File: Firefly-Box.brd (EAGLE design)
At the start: 90 x 56 mm, 40 parts, among them U1 ATMEGA32U4-XUMU, U2 ATMEGA32U4-XUAU, Y1 16MHz KX-7

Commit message: Add power to wings
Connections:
- removed net 5V: CONN2.VUSB, U1.7
- new net 5V0: AH1.5V@2, AH2.5V@2, AL1.5V@2, AL2.5V@2, BUS1.5V@2, BUS2.5V@2, BUS3.5V@2, BUS4.5V@2, CONN2.VUSB, U1.7
- net 3V3: now also AH1.3V3@2, AH2.3V3@2, AL1.3V3@2, AL2.3V3@2, BUS1.3V3@2, BUS2.3V3@2, BUS3.3V3@2, BUS4.3V3@2
- net GND: now also AH1.GND@2, AH2.GND@2, AL1.GND@2, AL2.GND@2, BUS1.GND@2, BUS2.GND@2, BUS3.GND@2, BUS4.GND@2
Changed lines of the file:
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@@
 </polygon>
 <contactref element="CONN2" pad="GND"/>
-<wire x1="33.909" y1="37.973" x2="34.544" y2="39.243" width="0" layer="19" extent="1-1"/>
-<wire x1="30.734" y1="41.021" x2="34.544" y2="39.243" width="0" layer="19" extent="1-1"/>
-<wire x1="19.177" y1="24.765" x2="21.184" y2="24.867" width="0" layer="19" extent="1-1"/>
-<wire x1="25.364" y1="40.887" x2="28.194" y2="39.116" width="0" layer="19" extent="1-1"/>
-<wire x1="27.214" y1="43.187" x2="25.364" y2="40.887" width="0" layer="19" extent="1-1"/>
-<wire x1="26.543" y1="45.212" x2="27.214" y2="43.187" width="0" layer="19" extent="1-1"/>
-<wire x1="15.24" y1="22.987" x2="19.177" y2="24.765" width="0" layer="19" extent="1-1"/>
-<wire x1="13.986" y1="25.908" x2="15.24" y2="22.987" width="0" layer="19" extent="1-1"/>
-<wire x1="33.274" y1="28.4376" x2="26.289" y2="28.067" width="0" layer="19" extent="16-16"/>
-<wire x1="8.95" y1="26.34" x2="15.24" y2="22.987" width="0" layer="19" extent="1-1"/>
-<wire x1="13.555" y1="36.322" x2="18.584" y2="33.972" width="0" layer="19" extent="1-1"/>
-<wire x1="13.555" y1="40.132" x2="13.555" y2="36.322" width="0" layer="19" extent="1-1"/>
+<contactref element="AH1" pad="GND@2"/>
+<contactref element="AL1" pad="GND@2"/>
+<contactref element="AL2" pad="GND@2"/>
+<contactref element="AH2" pad="GND@2"/>
+<contactref element="BUS2" pad="GND@2"/>
+<contactref element="BUS1" pad="GND@2"/>
+<contactref element="BUS3" pad="GND@2"/>
+<contactref element="BUS4" pad="GND@2"/>
 </signal>
 <signal name="AREF" class="4">
@@
 <contactref element="R5" pad="1"/>
 <contactref element="CONN2" pad="D+"/>
-<wire x1="8.95" y1="27.94" x2="7.89" y2="20.828" width="0" layer="19" extent="1-1"/>
+<wire x1="7.89" y1="20.828" x2="8.95" y2="27.94" width="0" layer="19" extent="1-1"/>
 </signal>
 <signal name="N$2">
@@
 <wire x1="30.184" y1="26.772" x2="29.362" y2="26.772" width="0.254" layer="1"/>
 <wire x1="25.884" y1="34.012" x2="25.884" y2="33.247" width="0.254" layer="1"/>
+<contactref element="BUS1" pad="3V3@2"/>
+<contactref element="BUS2" pad="3V3@2"/>
+<contactref element="BUS3" pad="3V3@2"/>
+<contactref element="BUS4" pad="3V3@2"/>
+<contactref element="AL2" pad="3V3@2"/>
+<contactref element="AH2" pad="3V3@2"/>
+<contactref element="AL1" pad="3V3@2"/>
+<contactref element="AH1" pad="3V3@2"/>
+<wire x1="53.848" y1="44.45" x2="74.168" y2="44.45" width="0" layer="19" extent="1-1"/>
+<wire x1="48.768" y1="34.29" x2="53.848" y2="44.45" width="0" layer="19" extent="1-1"/>
+<wire x1="41.148" y1="41.91" x2="48.768" y2="34.29" width="0" layer="19" extent="1-1"/>
+<wire x1="38.608" y1="41.656" x2="41.148" y2="41.91" width="0" layer="19" extent="1-1"/>
 <wire x1="27.659" y1="27.972" x2="25.884" y2="33.247" width="0" layer="19" extent="1-1"/>
 <wire x1="21.884" y1="26.697" x2="27.659" y2="27.972" width="0" layer="19" extent="1-1"/>
 <wire x1="21.884" y1="26.3544" x2="21.884" y2="26.697" width="0" layer="19" extent="1-1"/>
-<wire x1="12.192" y1="39.004" x2="26.784" y2="36.817" width="0" layer="19" extent="1-1"/>
+<wire x1="15.748" y1="11.43" x2="17.145" y2="22.86" width="0" layer="19" extent="1-1"/>
+<wire x1="41.148" y1="21.59" x2="30.184" y2="26.772" width="0" layer="19" extent="1-1"/>
+<wire x1="48.768" y1="13.97" x2="41.148" y2="21.59" width="0" layer="19" extent="1-1"/>
+<wire x1="36.068" y1="11.43" x2="41.148" y2="21.59" width="0" layer="19" extent="1-1"/>
+<wire x1="12.192" y1="39.004" x2="25.884" y2="34.012" width="0" layer="19" extent="1-1"/>
 <wire x1="10.668" y1="39.004" x2="12.192" y2="39.004" width="0" layer="19" extent="1-1"/>
 <wire x1="11.43" y1="41.672" x2="12.192" y2="39.004" width="0" layer="19" extent="1-1"/>
@@
 <wire x1="21.109" y1="28.972" x2="43.688" y2="19.05" width="0" layer="19" extent="1-1"/>
 </signal>
-<signal name="5V" class="3">
+<signal name="5V0">
+<contactref element="AH2" pad="5V@2"/>
+<contactref element="AL2" pad="5V@2"/>
+<contactref element="AL1" pad="5V@2"/>
+<contactref element="AH1" pad="5V@2"/>
+<contactref element="BUS3" pad="5V@2"/>
+<contactref element="BUS4" pad="5V@2"/>
+<contactref element="BUS2" pad="5V@2"/>
+<contactref element="BUS1" pad="5V@2"/>
 <contactref element="CONN2" pad="VUSB"/>
 <contactref element="U1" pad="7"/>
+<wire x1="56.388" y1="44.45" x2="76.708" y2="44.45" width="0" layer="19" extent="1-1"/>
+<wire x1="48.768" y1="36.83" x2="56.388" y2="44.45" width="0" layer="19" extent="1-1"/>
+<wire x1="41.148" y1="39.37" x2="48.768" y2="36.83" width="0" layer="19" extent="1-1"/>
+<wire x1="27.659" y1="30.472" x2="41.148" y2="39.37" width="0" layer="19" extent="1-1"/>
+<wire x1="41.148" y1="19.05" x2="27.659" y2="30.472" width="0" layer="19" extent="1-1"/>
+<wire x1="48.768" y1="16.51" x2="41.148" y2="19.05" width="0" layer="19" extent="1-1"/>
+<wire x1="33.528" y1="11.43" x2="41.148" y2="19.05" width="0" layer="19" extent="1-1"/>
 <wire x1="8.95" y1="29.54" x2="27.659" y2="30.472" width="0" layer="19" extent="1-1"/>
+<wire x1="13.208" y1="11.43" x2="8.95" y2="29.54" width="0" layer="19" extent="1-1"/>
 </signal>
 </signals>

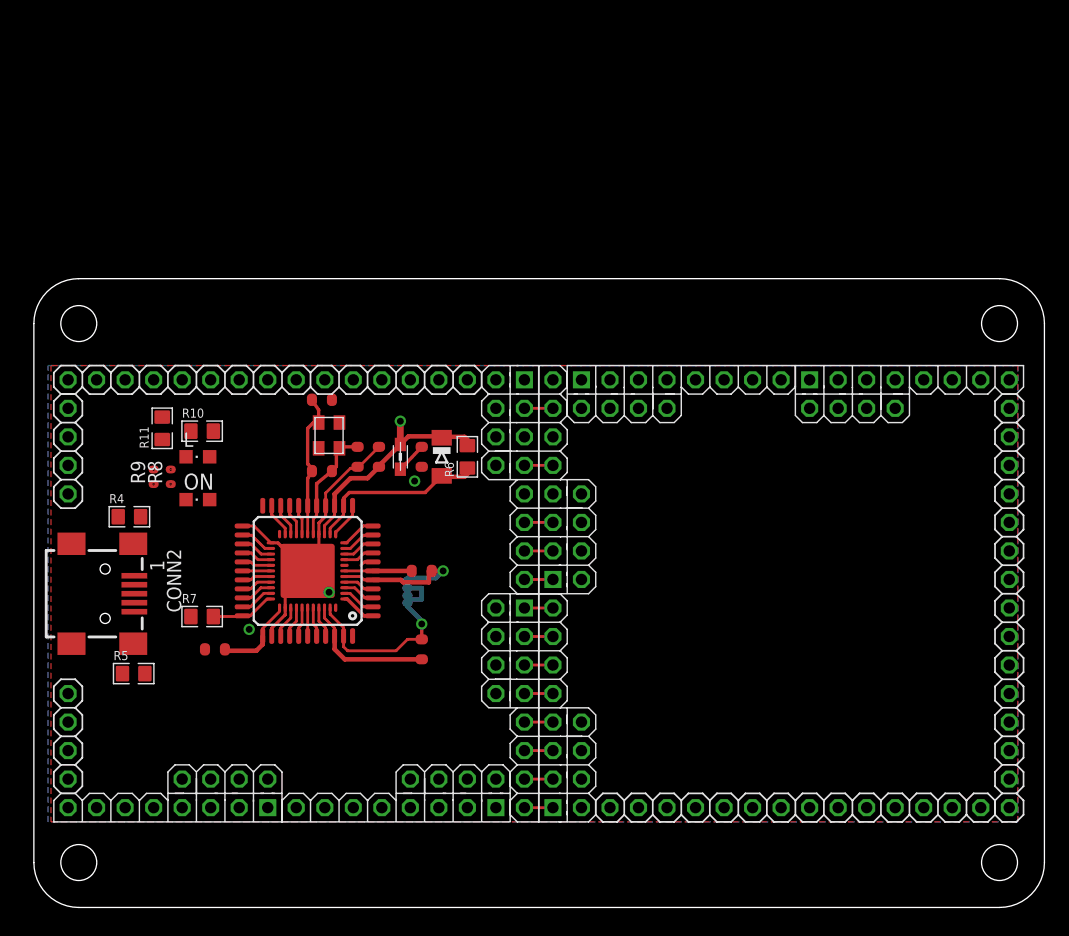
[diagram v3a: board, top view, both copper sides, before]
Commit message: Added Power and LiPo section.
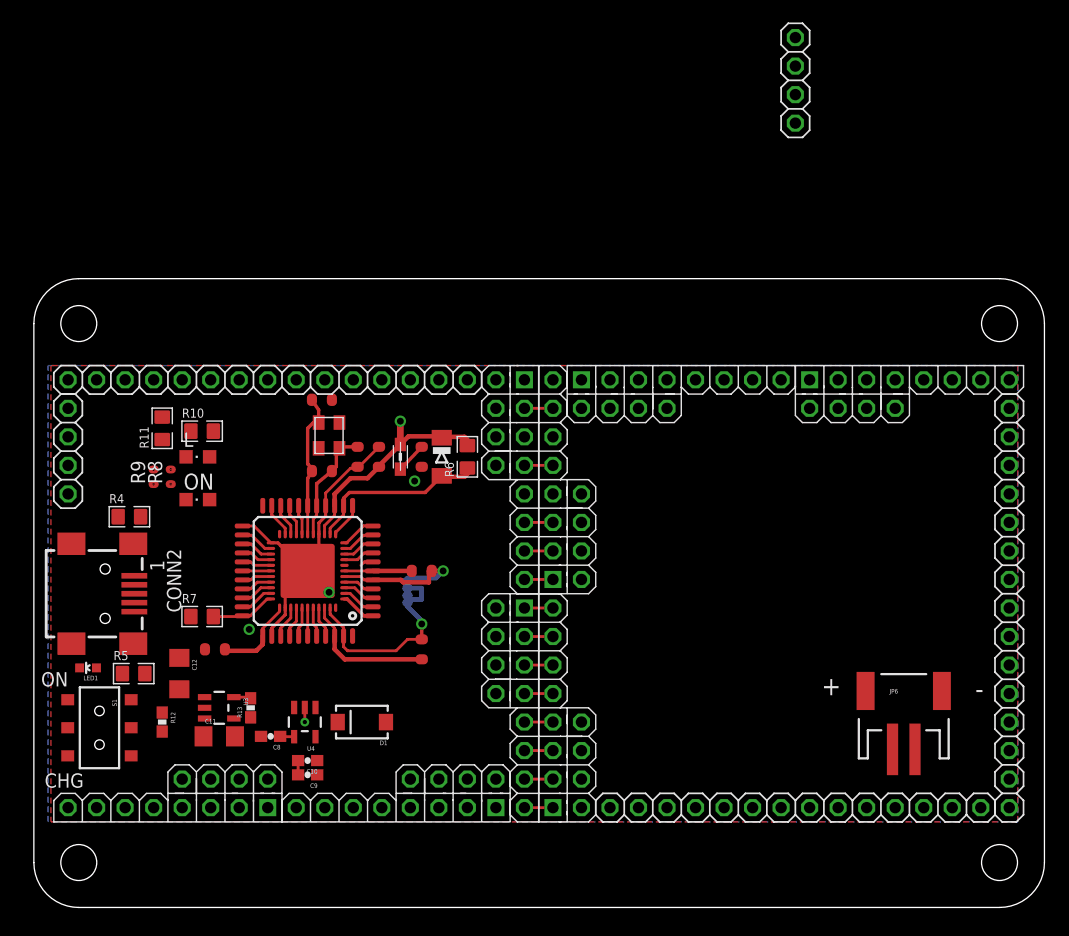
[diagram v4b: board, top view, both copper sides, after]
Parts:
- added C10: 4.7uF, SparkFun-Passives:0603-CAP
- added C11, C12: 4.7uF, SparkFun-Passives:1206
- added C8: 470pF, SparkFun-Passives:0603-CAP
- added C9: .1uF, SparkFun-Passives:0603-CAP
- added D1: B340A, SparkFun-DiscreteSemi:SMA-DIODE
- added JP6: JST-2, SparkFun-Connectors:JST-2-SMD
- added LED1: RED, SparkFun-LED:LED-0603
- added R12: 330, SparkFun-Passives:0603-RES
- added R13: 10k, SparkFun-Passives:0603-RES
- added S1: SWITCH-DPDTSMD, SparkFun-Electromechanical:AYZ0202
- added U3: MCP73831, SparkFun-PowerIC:SOT23-5
- added U4: MIC5219, SparkFun-PowerIC:SOT23-5
- moved JP5 87.2 mm to (67.8, 73.7)
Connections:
- new net N$1: S1.2, U4.3
- new net N$4: LED1.A, R12.1
- new net N$5: LED1.C, U3.1
- new net N$6: R13.2, U3.5
- new net N$8: C8.1, U4.4
- new net V_BATT: C12.2, D1.A, JP6.2, U3.3
- net 3V3: now also C10.2, C9.2, U4.5
- net 5V0: now also C11.2, D1.C, R12.2, S1.1, U3.4, U4.1
- net GND: now also C10.1, C11.1, C12.1, C8.2, C9.1, JP6.1, R13.1, S1.3, U3.2, U4.2
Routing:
- net N$8: track 0.00 -> 2.71 mm
- net 3V3: track 31.0 -> 32.5 mm
- net N$6: track 0.00 -> 1.51 mm
- net GND: track 35.9 -> 37.2 mm, vias 3 -> 4
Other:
- board text added: "+"
- board text added: "-"
- board text added: "CHG"
- board text added: "ON"

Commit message: Lots of routing done.
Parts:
- removed L: Yellow, led:CHIPLED_0805
- removed ON: Green, led:CHIPLED_0805
- removed R10, R11: 1K, GadgetFactory_6.0:0805
- moved R8 30.2 mm to (25.9, 11.4)
- moved R9 29.8 mm to (23.4, 11.4)
- moved R12 28.6 mm to (6.60, 44.7), turned to 0 degrees
- moved C9 27.8 mm to (19.4, 39.1), turned to 90 degrees
- moved C10 26.8 mm to (18.2, 39.1), turned to 90 degrees
- moved C11 26.0 mm to (14.2, 41.1)
- moved R13 26.0 mm to (17.0, 43.7)
- moved U3 26.0 mm to (14.2, 43.7)
- moved JP4 25.4 mm to (3.05, 15.2)
- moved D1 24.3 mm to (53.3, 14.0), turned to 270 degrees
- moved U4 23.8 mm to (14.2, 38.1), turned to 270 degrees
- moved LED1 23.4 mm to (3.56, 44.7)
- moved S1 22.9 mm to (5.33, 38.9)
- moved C12 22.0 mm to (10.4, 42.7)
- moved C8 21.7 mm to (14.2, 35.8)
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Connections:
- removed net N$2: L.A, R10.2
- removed net N$3: ON.A, R11.2
- removed net VUSB: U2.7
- net 3V3: no longer R11.1
- net 5V0: now also U2.7
- net D11*: now also AH1.5, AH2.2; no longer AH1.3, AH2.4
- net D12*: now also AL1.3, AL2.4; no longer AH1.4, AH2.3
- net D13*: now also AL1.4, AL2.3; no longer AH1.5, AH2.2
- net D3*: now also AH1.4, AH2.3; no longer AL1.3, AL2.4
- net D4*: now also AH1.3, AH2.4; no longer AL1.4, AL2.3, R10.1
- net GND: no longer L.C, ON.C
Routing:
- net SPI-CS4: track 0.00 -> 76.6 mm
- net 5V0: track 0.00 -> 73.8 mm, vias 0 -> 1
- net I2C-SCL: track 2.65 -> 64.8 mm, vias 0 -> 1
- net I2C-SDA: track 2.77 -> 59.7 mm, vias 0 -> 1
- net D15: track 5.07 -> 57.0 mm
- net RD+: track 2.77 -> 52.9 mm, vias 0 -> 2
- net AVCC: track 5.77 -> 53.5 mm, vias 0 -> 3
- net D12*: track 5.19 -> 51.2 mm, vias 0 -> 1
- net D11*: track 5.31 -> 49.2 mm
- net D3*: track 5.44 -> 47.5 mm
- net D13*: track 5.19 -> 46.3 mm, vias 0 -> 1
- net D4*: track 3.02 -> 42.4 mm
- net D0/RX: track 2.90 -> 42.0 mm, vias 0 -> 2
- net SPI-CS2: track 2.77 -> 41.5 mm, vias 0 -> 1
- net SPI-CS3: track 2.77 -> 40.9 mm, vias 0 -> 1
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- added copper zone on layer 1, net 3V3
- removed copper zone on layer 1, net GND

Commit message: Fully Routed
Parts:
- removed JP5: (no value), pinhead:1X04
- moved C10 0.72 mm to (17.7, 38.6)
- moved C9 0.51 mm to (19.4, 38.6)
- moved C11 0.25 mm to (14.2, 40.9)
- moved C12 0.25 mm to (10.4, 42.9)
- moved LED1 0.25 mm to (3.56, 44.5)
- moved R12 0.25 mm to (6.60, 44.5)
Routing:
- net SPI-MISO: track 3.15 -> 160.3 mm, vias 0 -> 5
- net I2C-SCL: track 64.8 -> 221.8 mm, vias 1 -> 7
- net V_BATT: track 3.12 -> 156.5 mm, vias 0 -> 4
- net 5V0: track 73.8 -> 223.0 mm, vias 1 -> 12
- net I2C-SDA: track 59.7 -> 196.3 mm, vias 1 -> 8
- net SPI-SCK: track 37.4 -> 173.6 mm, vias 0 -> 6
- net SPI-MOSI: track 32.4 -> 164.2 mm, vias 0 -> 2
- net 3V3: track 30.4 -> 96.3 mm, vias 1 -> 8
- net GND: track 74.5 -> 89.9 mm, vias 9 -> 14
- net D4*: track 42.4 -> 45.4 mm
- net SPI-CS4: track 76.6 -> 79.6 mm
- net SPI-CS3: track 40.9 -> 41.6 mm, vias 1 -> 3
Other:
- board text added: "TODO: Analog?"
- board text removed: "TODO: 3.3V Power Supply"
- board text removed: "TODO: MINI USB"
